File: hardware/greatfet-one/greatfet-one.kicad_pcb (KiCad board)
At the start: 4 copper layers, 70.6 x 53.3 mm, 98 parts, among them J1 NEIGHBOR1, J2 NEIGHBOR2, J3 USB-MICRO-B-SHIELDED, J4 USB-MICRO-B-SHIELDED, J5 JTAG, J6 POWER, J7 BONUS_ROW, SW1 DFU, SW2 RESET, U1 LPC4330FBD144, U2 W25Q16DV, U3 AP7333, U4 IP4220CZ6, U5 AP2553W6-7, X1 MCU_XTAL, X2 RTC_XTAL

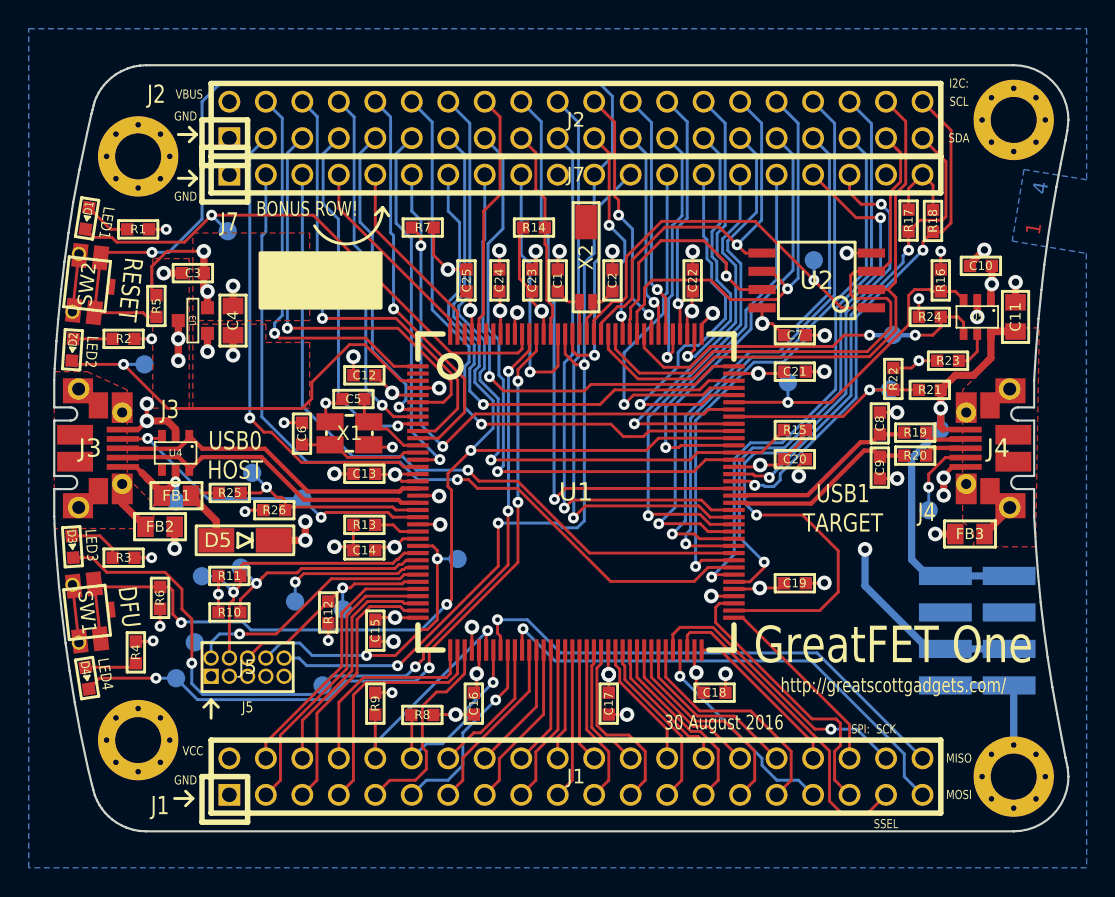
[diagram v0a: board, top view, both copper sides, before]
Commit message: GreatFET One: silkscreen update
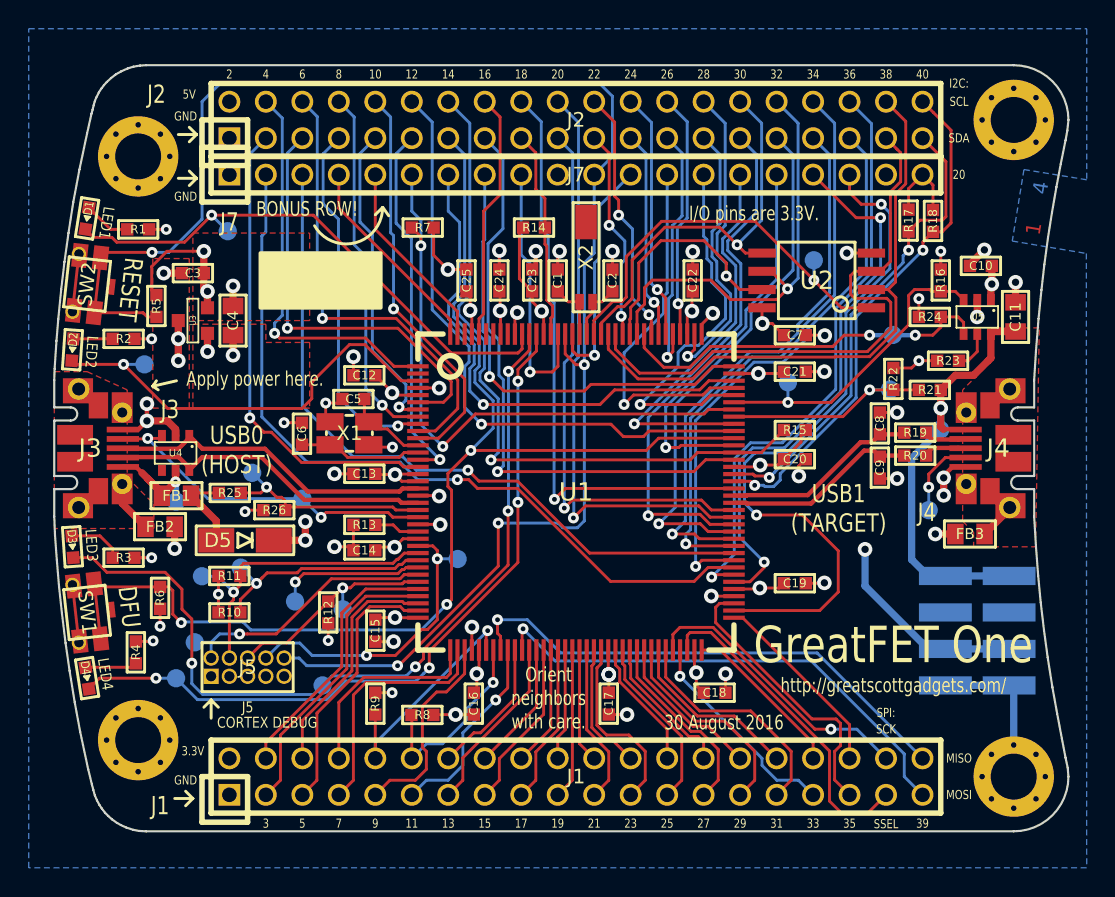
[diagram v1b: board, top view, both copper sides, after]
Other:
- board text added: "10"
- board text added: "11"
- board text added: "12"
- board text added: "13"
- board text added: "14"
- board text added: "15"
- board text added: "16"
- board text added: "17"
- board text added: "18"
- board text added: "19"
- board text added: "20"
- board text added: "21"
- board text added: "22"
- board text added: "23"
- board text added: "24"
- board text added: "25"
- board text added: "26"
- board text added: "27"
- board text added: "28"
- board text added: "29"
- board text added: "3.3V"
- board text added: "30"
- board text added: "31"
- board text added: "32"
- board text added: "33"
- board text added: "34"
- board text added: "35"
- board text added: "36"
- board text added: "38"
- board text added: "39"
- board text added: "40"
- board text added: "5"
- board text added: "5V"
- board text added: "6"
- board text added: "7"
- board text added: "8"
- board text added: "9"
- board text added: "Apply power here."
- board text added: "Be neighborly."
- board text added: "CORTEX DEBUG"
- board text added: "I/O pins are 3.3V."
- board text added: "J6"
- board text added: "Keep hacking."
- board text added: "Orient neighbors with care."
- board text added: "TP1 DBGEN"
- board text added: "TP10 USB1_EN"
- board text added: "TP11 USB1_FAULT"
- board text added: "TP12 USB1_ID"
- board text added: "TP13 USB0_ID"
- board text added: "TP14 USB0_VBUS"
- board text added: "TP15 USB0_SENSE"
- board text added: "TP16 TMS"
- board text added: "TP17 TCK"
- board text added: "TP18 TDO"
- board text added: "TP19 TDI"
- board text added: "TP2 TRST"
- board text added: "TP3 LED1"
- board text added: "TP4 LED2"
- board text added: "TP5 LED3"
- board text added: "TP6 LED4"
- board text added: "TP7 USB1_VBUS"
- board text added: "TP8 USB1_SENSE"
- board text added: "TP9 SPIFI_CS"
- board text added: "USB0 (HOST)"
- board text added: "USB1 (TARGET)"
- board text added: "USB1_VBUS"
- board text added: "Use lever to remove neighbors."
- board text removed: "USB0 HOST"
- board text removed: "USB1 TARGET"
- board text removed: "VBUS"
- board text removed: "VCC"

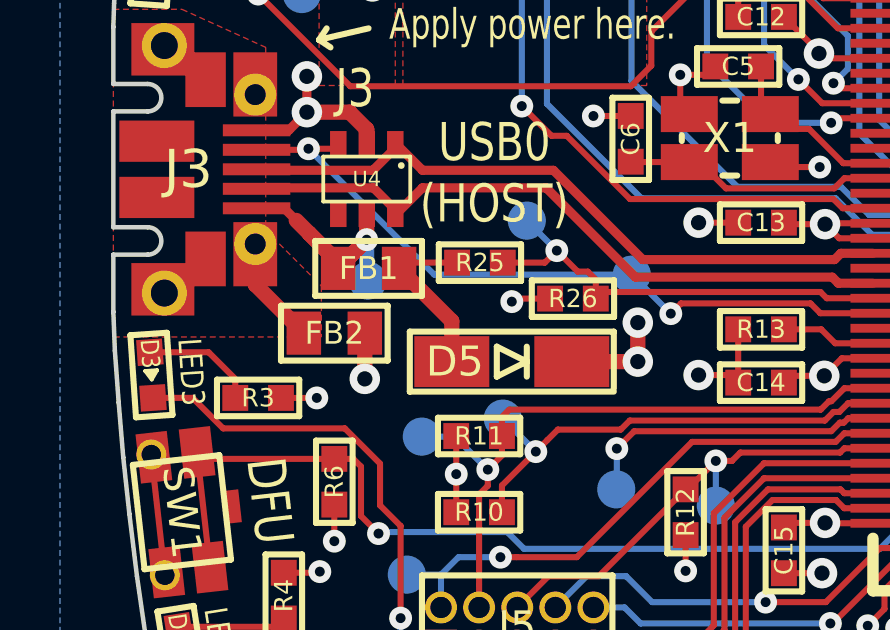
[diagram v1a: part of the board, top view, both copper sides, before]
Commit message: GreatFET One: solder jumper to bypass VBUS diode
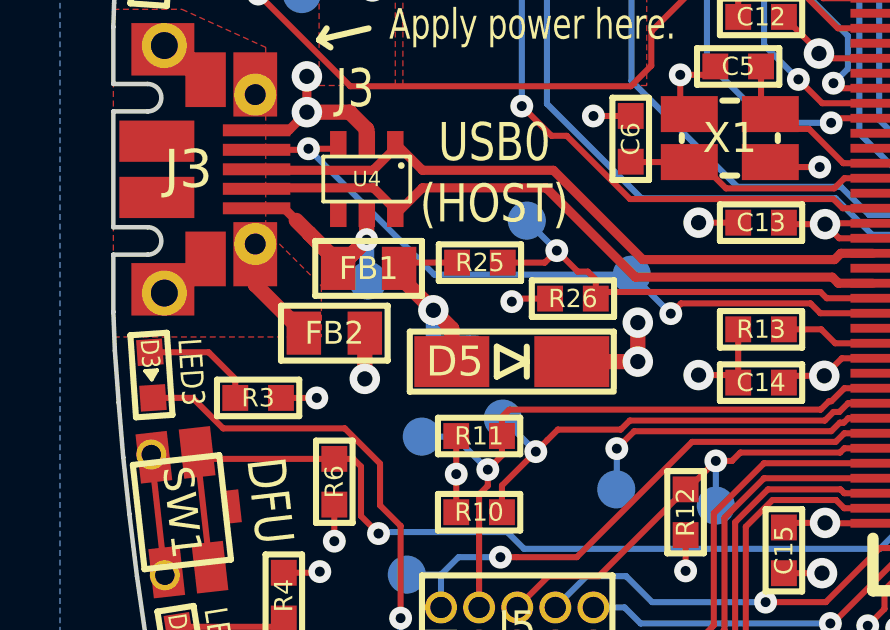
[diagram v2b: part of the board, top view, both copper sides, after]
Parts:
- added W1: VBUS_BYPASS, gsg-modules:0603-JUMPER, B.Cu at (117.2, 103.8)
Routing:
- net Net-(D5-Pad2): track 5.85 -> 7.12 mm, vias 0 -> 1
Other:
- board text added: "W1 VBUS_BYPASS"
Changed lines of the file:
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@@
 (kicad_pcb (version 4) (host pcbnew "(2015-08-18 BZR 6102)-product")
   (general
-    (links 370)
+    (links 374)
     (no_connects 0)
-    (area 93.271704 68.58 207.466001 199.465001)
+    (area 105.842999 71.044999 176.605001 124.535001)
     (thickness 1.6)
-    (drawings 227)
-    (tracks 1522)
+    (drawings 228)
+    (tracks 1526)
     (zones 0)
-    (modules 98)
+    (modules 99)
     (nets 141)
   )
@@
   (layers
     (0 F.Cu signal)
-    (1 C2.Cu power)
-    (2 C3.Cu power)
+    (1 C2.Cu power hide)
+    (2 C3.Cu power hide)
     (31 B.Cu signal)
     (32 B.Adhes user)
@@
   )
   (setup
-    (last_trace_width 0.2032)
+    (last_trace_width 0.508)
     (user_trace_width 0.3048)
     (user_trace_width 0.508)
@@
     (pad_to_paste_clearance_ratio -0.05)
     (aux_axis_origin 0 0)
-    (visible_elements FFFFBF7F)
+    (visible_elements FFFFFF7F)
     (pcbplotparams
       (layerselection 0x010f8_80000007)
@@
       (net 7 /USB1_VBUS))
   )
+  (module gsg-modules:0603-JUMPER (layer B.Cu)
+    (at 117.2337 103.759 180)
+    (solder_mask_margin 0.1016)
+    (fp_text reference W1 (at 0 0 180) (layer B.SilkS)
+      (effects (font (size 0.6096 0.6096) (thickness 0.1524)) (justify mirror))
+    )
+    (fp_text value VBUS_BYPASS (at 0 0 180) (layer B.SilkS) hide
+      (effects (font (size 0.6096 0.6096) (thickness 0.1524)) (justify mirror))
+    )
+    (fp_line (start -0.762 -0.6096) (end 0.762 -0.6096) (layer B.SilkS) (width 0.15))
+    (fp_line (start 0.762 0.6096) (end -0.762 0.6096) (layer B.SilkS) (width 0.15))
+    (fp_arc (start 0.762 0) (end 0.762 0.6096) (angle -180) (layer B.SilkS) (width 0.15))
+    (fp_arc (start -0.762 0) (end -0.762 -0.6096) (angle -180) (layer B.SilkS) (width 0.15))
+    (pad 1 smd oval (at -0.6477 0 180) (size 1.0922 0.8636) (layers B.Cu B.Mask)
+      (net 137 +5V) (solder_mask_margin 0.1016) (clearance 0.1778))
+    (pad 2 smd rect (at 0.3556 0 180) (size 0.508 0.8636) (layers B.Cu B.Mask)
+      (net 138 "Net-(D5-Pad2)") (solder_mask_margin 0.1016) (clearance 0.1778))
+    (pad 1 smd rect (at -0.3556 0 180) (size 0.508 0.8636) (layers B.Cu B.Mask)
+      (net 137 +5V) (solder_mask_margin 0.1016) (clearance 0.1778))
+    (pad 2 smd oval (at 0.6477 0 180) (size 1.0922 0.8636) (layers B.Cu B.Mask)
+      (net 138 "Net-(D5-Pad2)"))
+  )
+  (gr_text "W1\nVBUS_BYPASS" (at 112.649 103.124) (layer B.SilkS)
+    (effects (font (size 0.635 0.508) (thickness 0.1016)) (justify mirror))
+  )
   (gr_text "Use lever\nto remove\nneighbors." (at 141.224 96.266) (layer B.SilkS)
     (effects (font (size 1.27 1.016) (thickness 0.1524)) (justify mirror))
@@
     (effects (font (size 1.27 1.016) (thickness 0.1524)) (justify mirror))
   )
-  (gr_text "TP14\nUSB0_VBUS" (at 112.522 102.743) (layer B.SilkS)
+  (gr_text "TP14\nUSB0_VBUS" (at 114.427 98.679) (layer B.SilkS)
     (effects (font (size 0.635 0.508) (thickness 0.1016)) (justify mirror))
   )
@@
   (segment (start 171.13 86.426) (end 171.196 86.36) (width 0.3048) (layer F.Cu) (net 137))
   (via (at 171.196 86.36) (size 1.016) (drill 0.508) (layers F.Cu B.Cu) (net 137))
-  (segment (start 117.2 104.2) (end 117.2 102.849) (width 0.508) (layer F.Cu) (net 138))
-  (segment (start 117.2 102.849) (end 115.443 101.092) (width 0.508) (layer F.Cu) (net 138))
+  (segment (start 116.586 103.759) (end 116.586 102.489) (width 0.508) (layer B.Cu) (net 138))
+  (segment (start 115.443 101.092) (end 115.443 101.346) (width 0.508) (layer F.Cu) (net 138))
+  (segment (start 115.443 101.346) (end 116.586 102.489) (width 0.508) (layer F.Cu) (net 138))
+  (segment (start 117.2 104.2) (end 117.2 103.103) (width 0.508) (layer F.Cu) (net 138))
+  (segment (start 117.2 103.103) (end 116.586 102.489) (width 0.508) (layer F.Cu) (net 138))
+  (via (at 116.586 102.489) (size 1.016) (drill 0.508) (layers F.Cu B.Cu) (net 138))
   (segment (start 117.376 100.9) (end 115.635 100.9) (width 0.2032) (layer F.Cu) (net 138))
   (segment (start 115.635 100.9) (end 115.443 101.092) (width 0.2032) (layer F.Cu) (net 138))

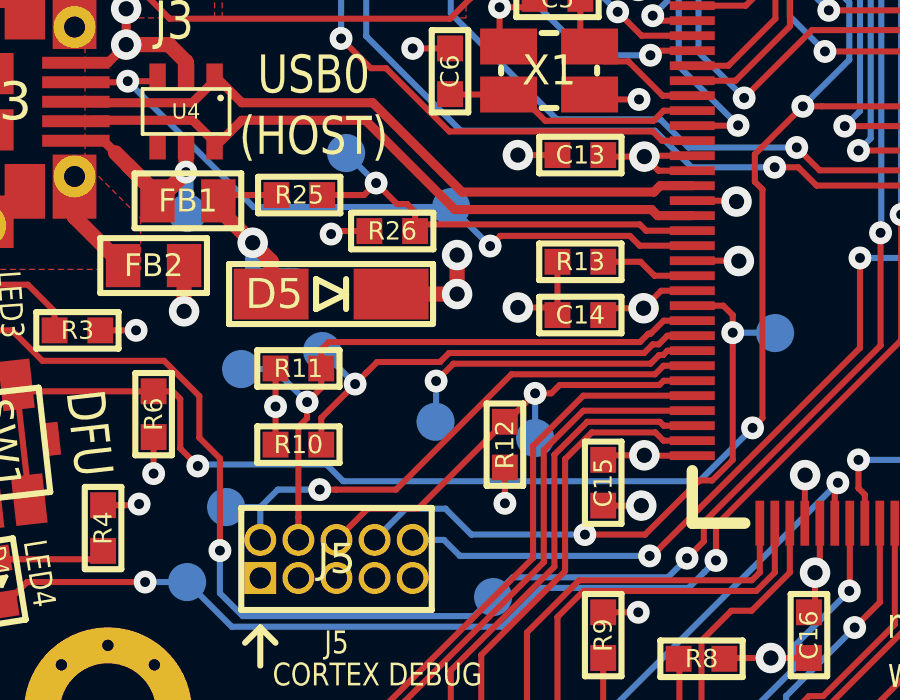
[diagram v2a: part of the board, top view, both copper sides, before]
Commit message: GreatFET One: replaced D5 with a part with lower forward voltage to maximize the usefulness of +5V for USB1 and neighbors
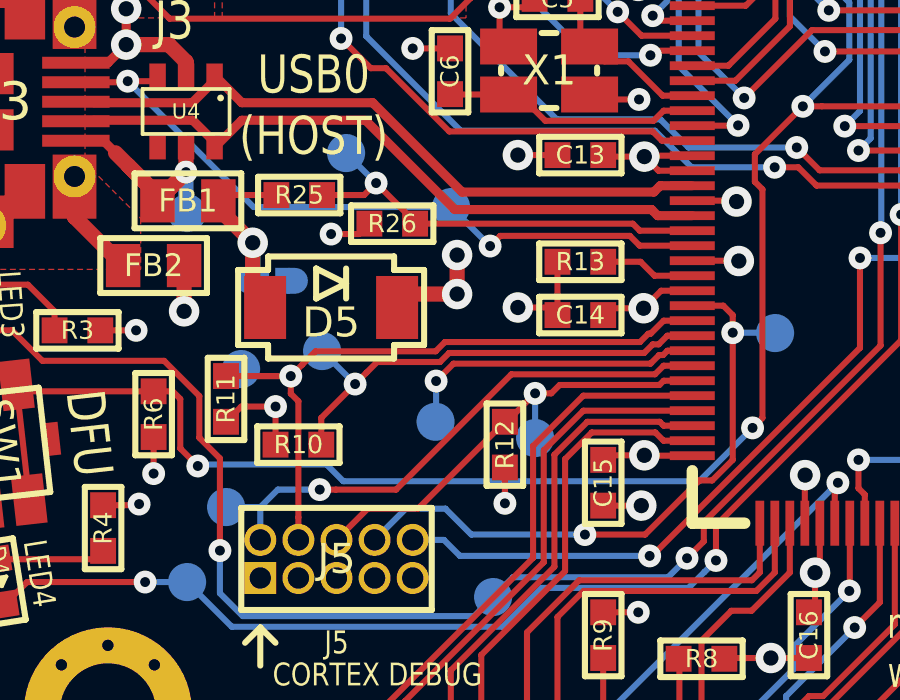
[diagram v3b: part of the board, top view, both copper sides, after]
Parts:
- D5: footprint gsg-modules:B140-13-F -> gsg-modules:SOD128
- moved R11 2.62 mm to (115.7, 107.7), turned to 90 degrees
- moved D5 0.45 mm to (119.2, 104.6)
- moved R26 0.25 mm to (121.2, 101.9)
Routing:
- net /TCK: track 22.1 -> 23.6 mm
- net VCC: track 103.3 -> 103.9 mm
- net /USB0_SENSE: track 15.1 -> 14.6 mm
